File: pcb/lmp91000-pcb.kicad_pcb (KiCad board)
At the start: 4 copper layers, 30 x 30 mm, 53 parts, among them J1 TC2030, J2 UJC-H-G-SMT-2-P6-TR, J3 0530480210, J4 TB0011-350-03GR, J5 0528070310, Q1 NTR4003N, SW1 PTS815SJM250SMTRLFS, U1 2450AT18D0100001E, U2 EFR32BG24L210F768IM40-B, U3 MCP73811T-420I-OT, U4 TLV77133PDBVR, U5 LMP91000SDX/NOPB, U6 LSM6DSV, Y1 XTL501250-S315-038

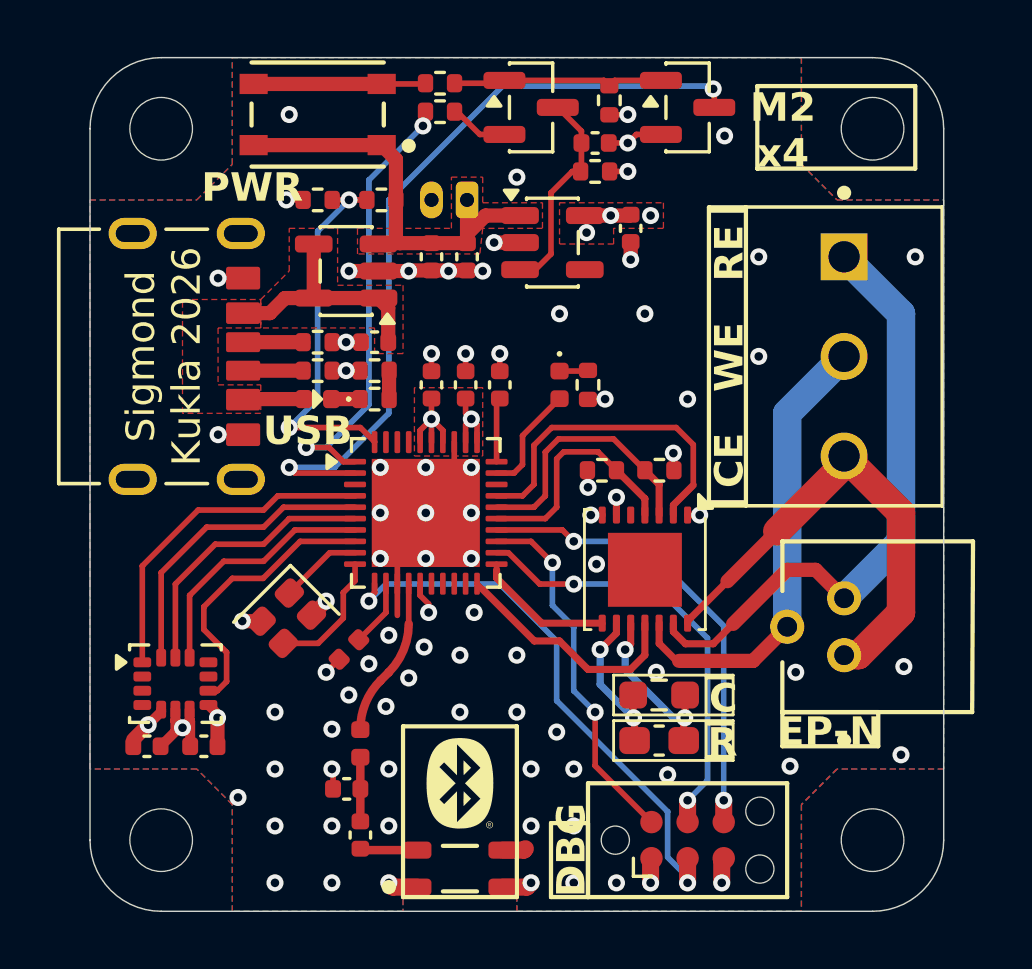
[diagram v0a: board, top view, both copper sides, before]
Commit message: add c1 and int1 to pcb
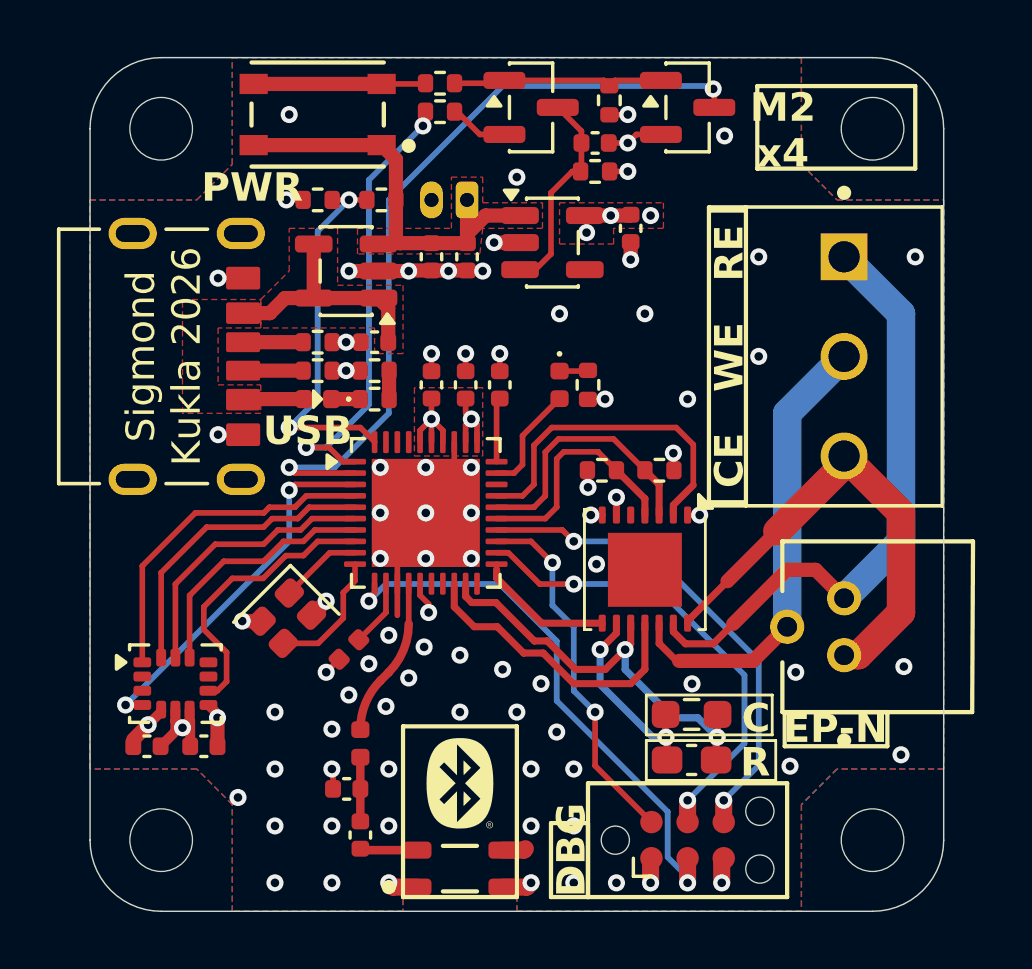
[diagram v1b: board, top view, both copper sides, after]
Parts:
- moved C12 1.33 mm to (106.1, 74.7)
- moved R12 1.33 mm to (106.1, 73.1)
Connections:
- C12 pad 1: Net-(U5-C1) -> /C1
- R12 pad 1: Net-(U5-C1) -> /C1
- U2 pad 18: unconnected-(U2-PB02-Pad18) -> /LMP_VREF
- U2 pad 19: unconnected-(U2-PB01-Pad19) -> /C1
- U2 pad 20: /LMP_VREF -> unconnected-(U2-PB00-Pad20)
- U2 pad 3: unconnected-(U2-PC02-Pad3) -> /IMU_INT1
- U5 pad 10: Net-(U5-C1) -> /C1
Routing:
- net /C1: track 0.00 -> 14.9 mm, vias 0 -> 2
- net /IMU_INT1: track 0.00 -> 13.1 mm, vias 0 -> 2
- net Net-(U5-C1): track 6.13 -> 0.00 mm, vias 2 -> 0
- net /LMP_VREF: track 8.48 -> 10.5 mm
- net Net-(U5-C2): track 5.67 -> 7.02 mm
- net /SWCLK: track 15.4 -> 16.5 mm
- net /SWV/SWO: track 16.3 -> 17.3 mm
- net GND: vias 80 -> 79

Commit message: Redesign for board order. add LFXO and shield electrode traces better
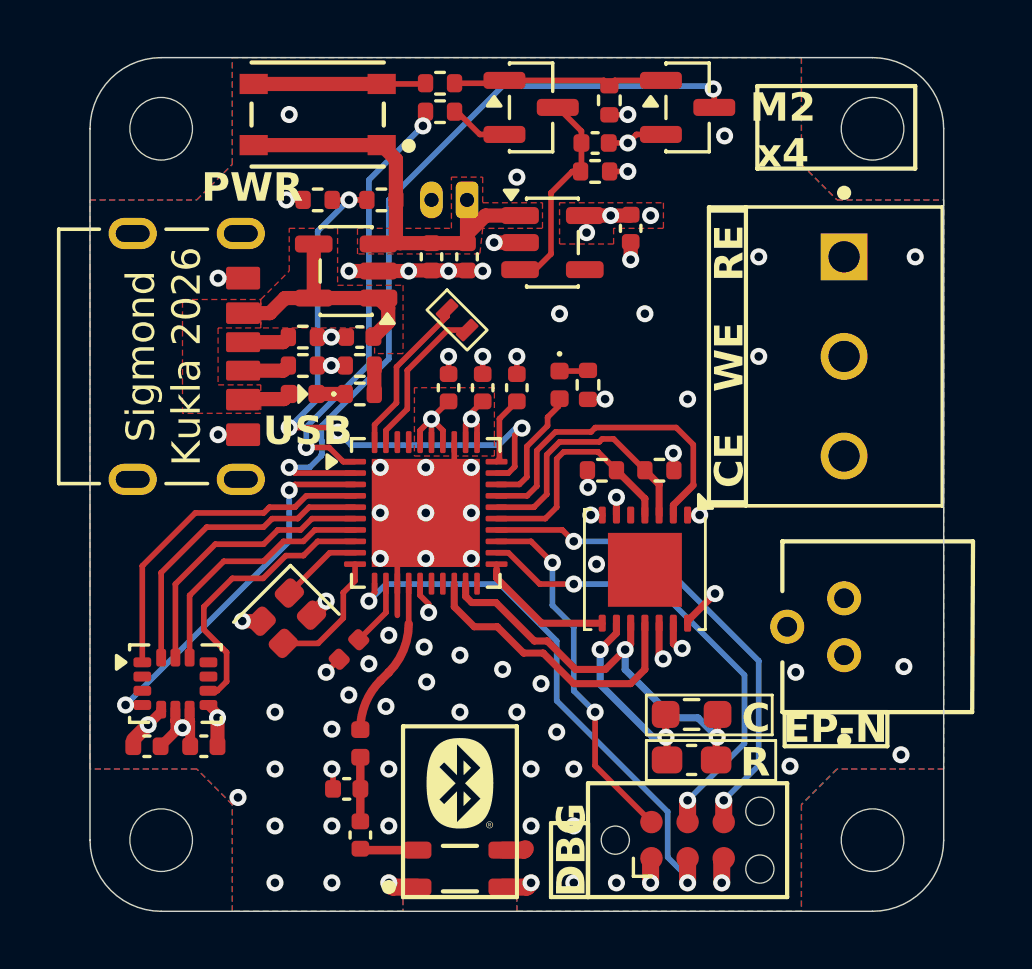
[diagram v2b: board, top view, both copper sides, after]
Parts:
- added Y2: Crystal, crystal_smd_dst1610a:KDS-DST1610A, F.Cu at (98.3, 59.6)
- moved C1 0.61 mm to (97.6, 61.6)
- moved C2 0.61 mm to (98.8, 61.6)
- moved C6 0.61 mm to (100.0, 61.6)
- moved C9 0.55 mm to (94.5, 59.8)
- moved D2 0.55 mm to (92.5, 61.8)
- moved R13 0.55 mm to (94.5, 60.8)
- moved R4 0.55 mm to (92.5, 60.8)
- moved R5 0.55 mm to (92.5, 59.8)
- moved R7 0.55 mm to (94.5, 61.8)
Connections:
- U2 pad 28: unconnected-(U2-PA07-Pad28) -> /LED
- U2 pad 29: /LED -> /BATT_MEAS
- U2 pad 39: unconnected-(U2-PD01-Pad39) -> /LFXTAL_I
- U2 pad 40: /BATT_MEAS -> /LFXTAL_O
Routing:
- net /BATT_MEAS: track 13.3 -> 21.0 mm, vias 2 -> 4
- net /LFXTAL_O: track 0.00 -> 5.70 mm
- net /LFXTAL_I: track 0.00 -> 5.52 mm
- net /LMP/WE: track 16.3 -> 17.0 mm, vias 0 -> 1
- net /LED: track 3.89 -> 4.40 mm
- net /LMP/CE: track 17.1 -> 16.6 mm, vias 0 -> 1
- net /LMP/RE: track 21.6 -> 22.0 mm, vias 0 -> 1
- net GND: vias 79 -> 78
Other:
- board text added: "v1.1"
- board text removed: "v1.0"

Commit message: Update Gerbers for release
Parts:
- moved D2 5.11 mm to (97.1, 59.6)
- moved R13 5.11 mm to (99.1, 58.6)
- moved R7 5.11 mm to (99.1, 59.6)
- moved Y2 3.23 mm to (95.7, 61.5), turned to 180 degrees
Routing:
- net /LFXTAL_O: track 5.70 -> 2.13 mm
- net /LFXTAL_I: track 5.52 -> 2.11 mm
- net GND: track 29.2 -> 29.8 mm, vias 78 -> 81
